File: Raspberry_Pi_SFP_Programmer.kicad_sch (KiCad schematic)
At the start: 18 parts, among them J1 RPi_GPIO, J2 SFP+, J4 Conn_02x03_Odd_Even, Q1 BC847, Q2 BC847

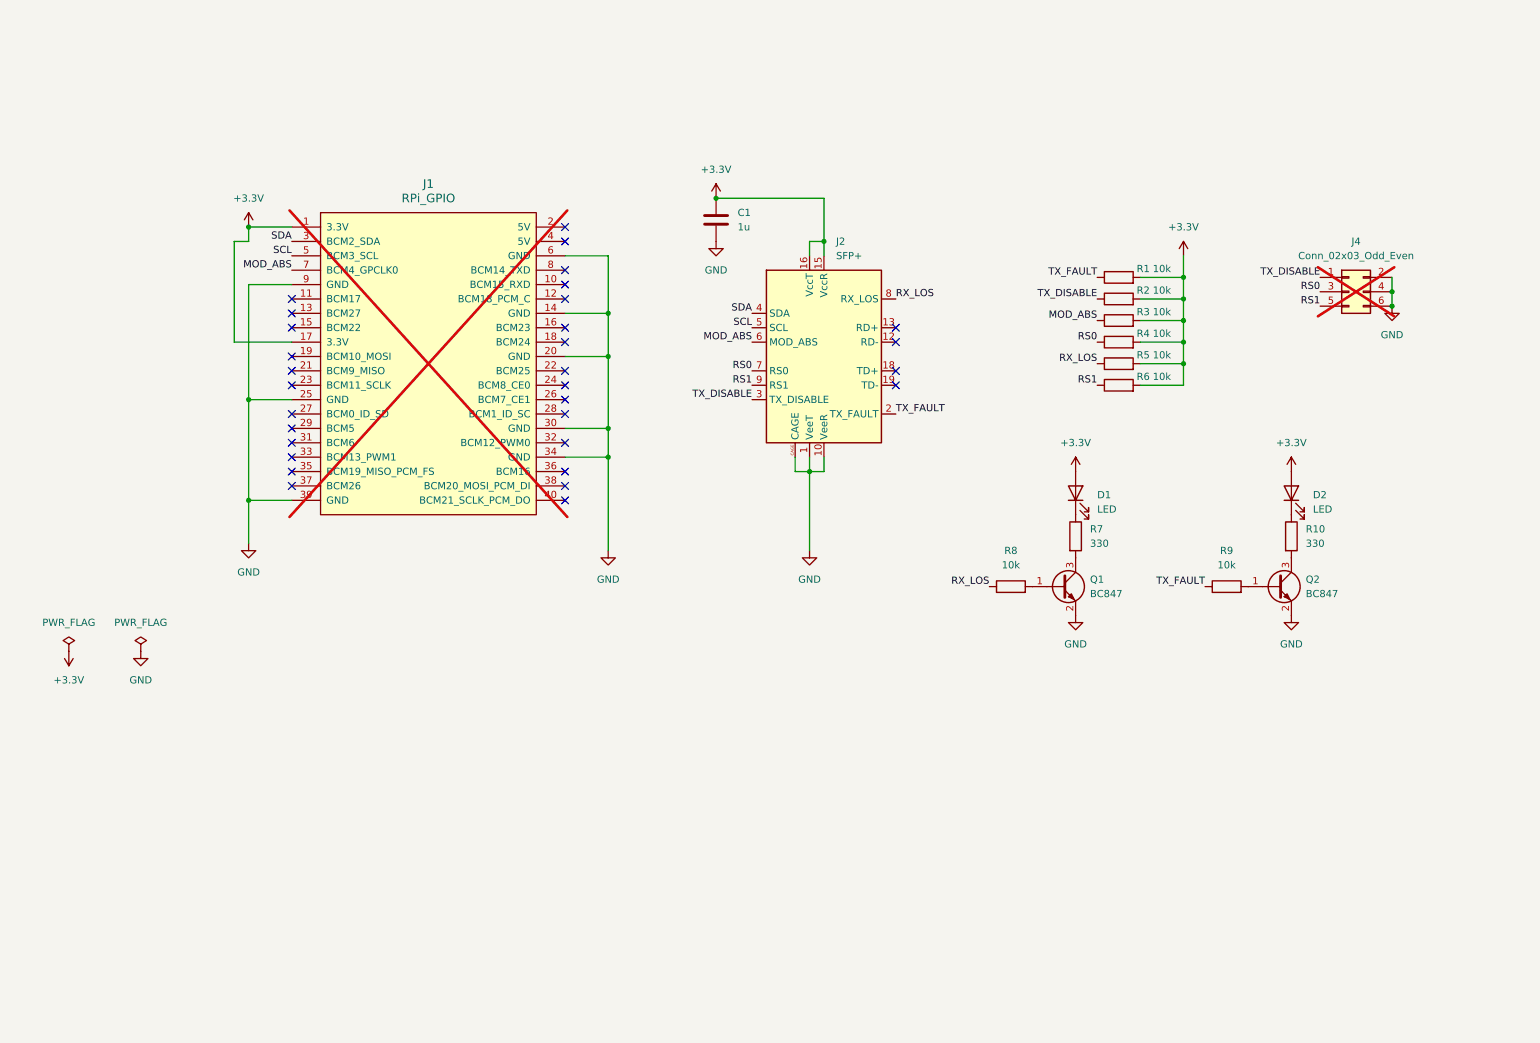
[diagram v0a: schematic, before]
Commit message: Multiple improvements
Fix 3.3V rail decoupling
Derive VccT and VccR from 5V
Add power supply filter networks
Replace jumper pin header with dip switch
Add LED for MOD_ABS
Connect RX_LOS and TX_FAULT to GPIOs
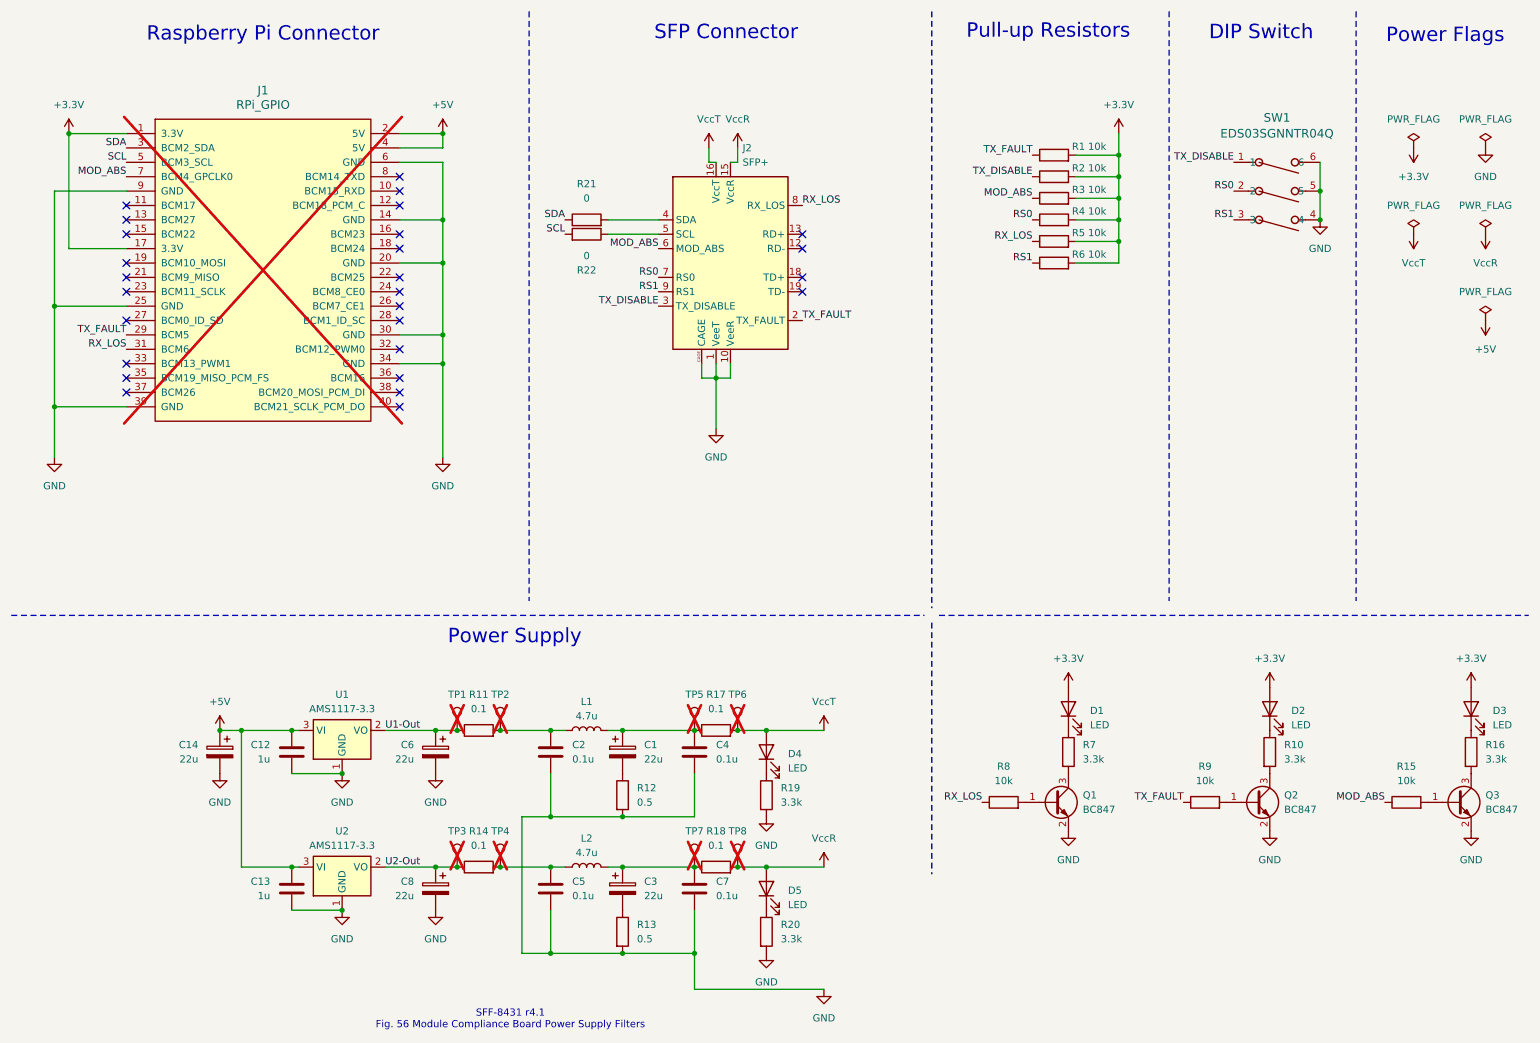
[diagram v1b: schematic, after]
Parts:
- removed C1: 1u, Capacitor_SMD:C_0402_1005Metric_Pad0.74x0.62mm_HandSolder, symbol Device:C
- removed J4: Conn_02x03_Odd_Even, Connector_PinHeader_2.54mm:PinHeader_2x03_P2.54mm_Vertical, symbol Connector_Generic:Conn_02x03_Odd_Even
- added C1, C14, C3, C6, C8: 22u, Capacitor_Tantalum_SMD:CP_EIA-3528-21_Kemet-B_HandSolder, symbol Device:C_Polarized
- added C12, C13: 1u, Capacitor_SMD:C_0603_1608Metric_Pad1.08x0.95mm_HandSolder, symbol Device:C
- added C2, C4, C5, C7: 0.1u, Capacitor_SMD:C_0402_1005Metric_Pad0.74x0.62mm_HandSolder, symbol Device:C
- added D3, D4, D5: LED, LED_SMD:LED_0402_1005Metric_Pad0.77x0.64mm_HandSolder, symbol Device:LED
- added L1, L2: 4.7u, Inductor_SMD:L_0805_2012Metric_Pad1.05x1.20mm_HandSolder, symbol Device:L
- added Q3: BC847, Package_TO_SOT_SMD:SOT-23, symbol Transistor_BJT:BC847
- added R11, R14, R17, R18: 0.1, Resistor_SMD:R_0805_2012Metric_Pad1.20x1.40mm_HandSolder, symbol Device:R
- added R12, R13: 0.5, Resistor_SMD:R_0402_1005Metric_Pad0.72x0.64mm_HandSolder, symbol Device:R
- added R15: 10k, Resistor_SMD:R_0402_1005Metric_Pad0.72x0.64mm_HandSolder, symbol Device:R
- added R16, R19, R20: 3.3k, Resistor_SMD:R_0402_1005Metric_Pad0.72x0.64mm_HandSolder, symbol Device:R
- added R21, R22: 0, Resistor_SMD:R_0402_1005Metric_Pad0.72x0.64mm_HandSolder, symbol Device:R
- added SW1: EDS03SGNNTR04Q, Raspberry_Pi_SFP_Programmer:SW_2319847_TEC, symbol Raspberry_Pi_SFP_Programmer:EDS03SGNNTR04Q
- added TP1, TP2, TP3, TP4, TP5, TP6, TP7, TP8: TestPoint, TestPoint:TestPoint_Pad_D1.0mm, symbol Connector:TestPoint
- added U1, U2: AMS1117-3.3, Package_TO_SOT_SMD:SOT-223-3_TabPin2, symbol Regulator_Linear:AMS1117-3.3
- D1, D2: JLCPCB Part # (none) -> C5123485
- J2: JLCPCB Part # (none) -> C42931381; LCSC Part Number C42931381 -> (none)
- Q1, Q2: JLCPCB Part # (none) -> C8664
- R1, R2, R3, R4, R5, R6, R8, R9: JLCPCB Part # (none) -> C60490; LCSC Part Number C60490 -> (none)
- R10, R7: value 330 -> 3.3k; JLCPCB Part # (none) -> C25936
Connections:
- net +3.3V: now also D3.2 (A); no longer J2.15 (VccR), J2.16 (VccT)
- net GND: now also C12.1, C13.1, C14.2, C2.2, C4.2, C5.2, C6.2, C7.2, C8.2, Q3.2 (E), R12.2, R13.2, R19.2, R20.2, SW1.4, SW1.5, SW1.6, U1.1 (GND), U2.1 (GND)
- net MOD_ABS: now also R15.1
- net RS0: now also SW1.2
- net RS1: now also SW1.3
- net RX_LOS: now also J1.31 (BCM6)
- net SCL: now also R22.2; no longer J2.5 (SCL)
- net SDA: now also R21.1; no longer J2.4 (SDA)
- net TX_DISABLE: now also SW1.1
- net TX_FAULT: now also J1.29 (BCM5)
- net +5V: now reaches J1.2 (5V)
- net +5V: now also J1.4 (5V), C12.2, C13.2, C14.1, U1.3 (VI), U2.3 (VI)
- new net: C5.1, L2.1, R14.2, TP4.1
- new net: C2.1, L1.1, R11.2, TP2.1
- new net: C3.1, C7.1, L2.2, R18.1, TP7.1
- new net: C3.2, R13.1
- new net: D5.1 (K), R20.1
- new net: D3.1 (K), R16.1
- new net: Q3.3 (C), R16.2
- new net: C1.2, R12.1
- new net: Q3.1 (B), R15.2
- new net: J2.4 (SDA), R21.2
- new net: J2.5 (SCL), R22.1
- new net: D4.1 (K), R19.1
- new net: C1.1, C4.1, L1.2, R17.1, TP5.1
- new net U1-Out: C6.1, R11.1, TP1.1, U1.2 (VO)
- new net U2-Out: C8.1, R14.1, TP3.1, U2.2 (VO)
- new net VccR: D5.2 (A), J2.15 (VccR), R18.2, TP8.1
- new net VccT: D4.2 (A), J2.16 (VccT), R17.2, TP6.1
- no-connect marks 31 -> 27
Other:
- note added: "DIP Switch"
- note added: "Power Flags"
- note added: "Power Supply"
- note added: "Pull-up Resistors"
- note added: "Raspberry Pi Connector"
- note added: "SFF-8431 r4.1 Fig. 56 Module Compliance Board Power Supply Filters"
- note added: "SFP Connector"
- company: (none) -> Author: Alexander "blackbit" Huemer
- title: (none) -> Raspberry Pi SFP Programmer
- moved on the sheet: D1, D2, J1, J2, Q1, Q2, R1, R10, R2, R3, R4, R5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
